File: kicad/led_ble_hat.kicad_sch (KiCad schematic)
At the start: 73 parts, among them J1 USB_C_Receptacle_USB2.0_14P, J2 Battery, J3 Prog, J4 DEBUG, J5 Strip, Q1 2N7002, Q2 AO3401A, Q3 2N7002, Q4 AO3401A, Q5 2N7002, Q6 2N7002, Q7 BSS84, Q8 BSS84, SW1 SW-18010P, U1 TP4054, U2 XC6206P332MR, U3 STM32WB55CGUx, Y1 32Mhz

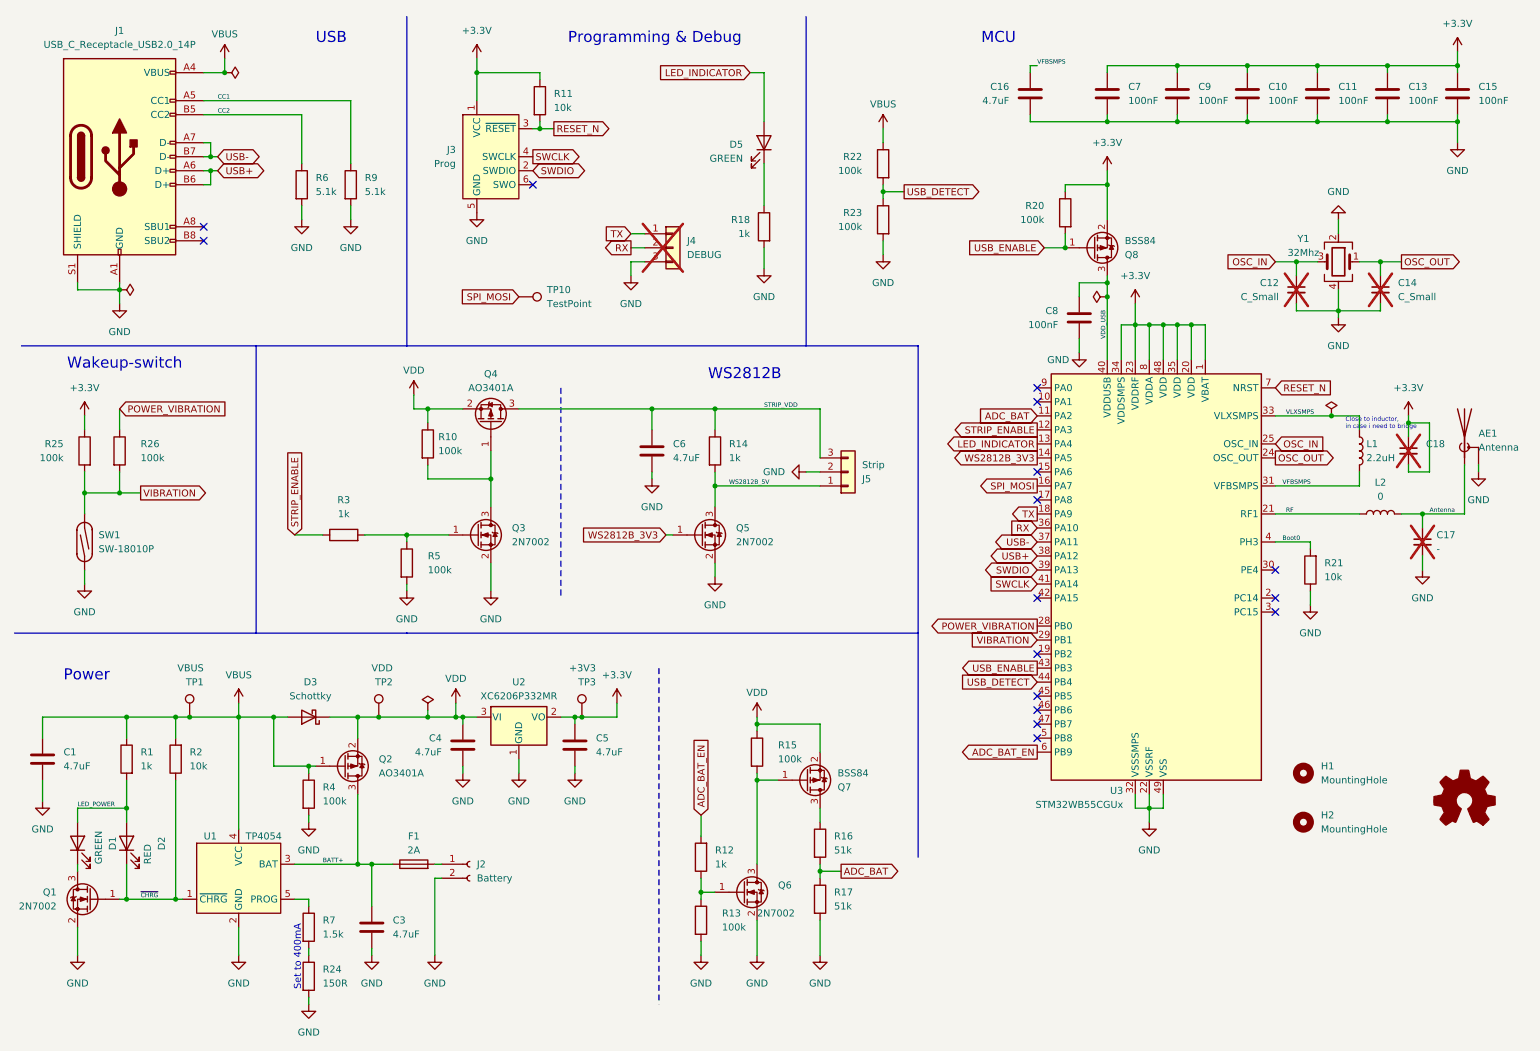
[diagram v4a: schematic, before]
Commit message: Add double inverter for ws2812b output
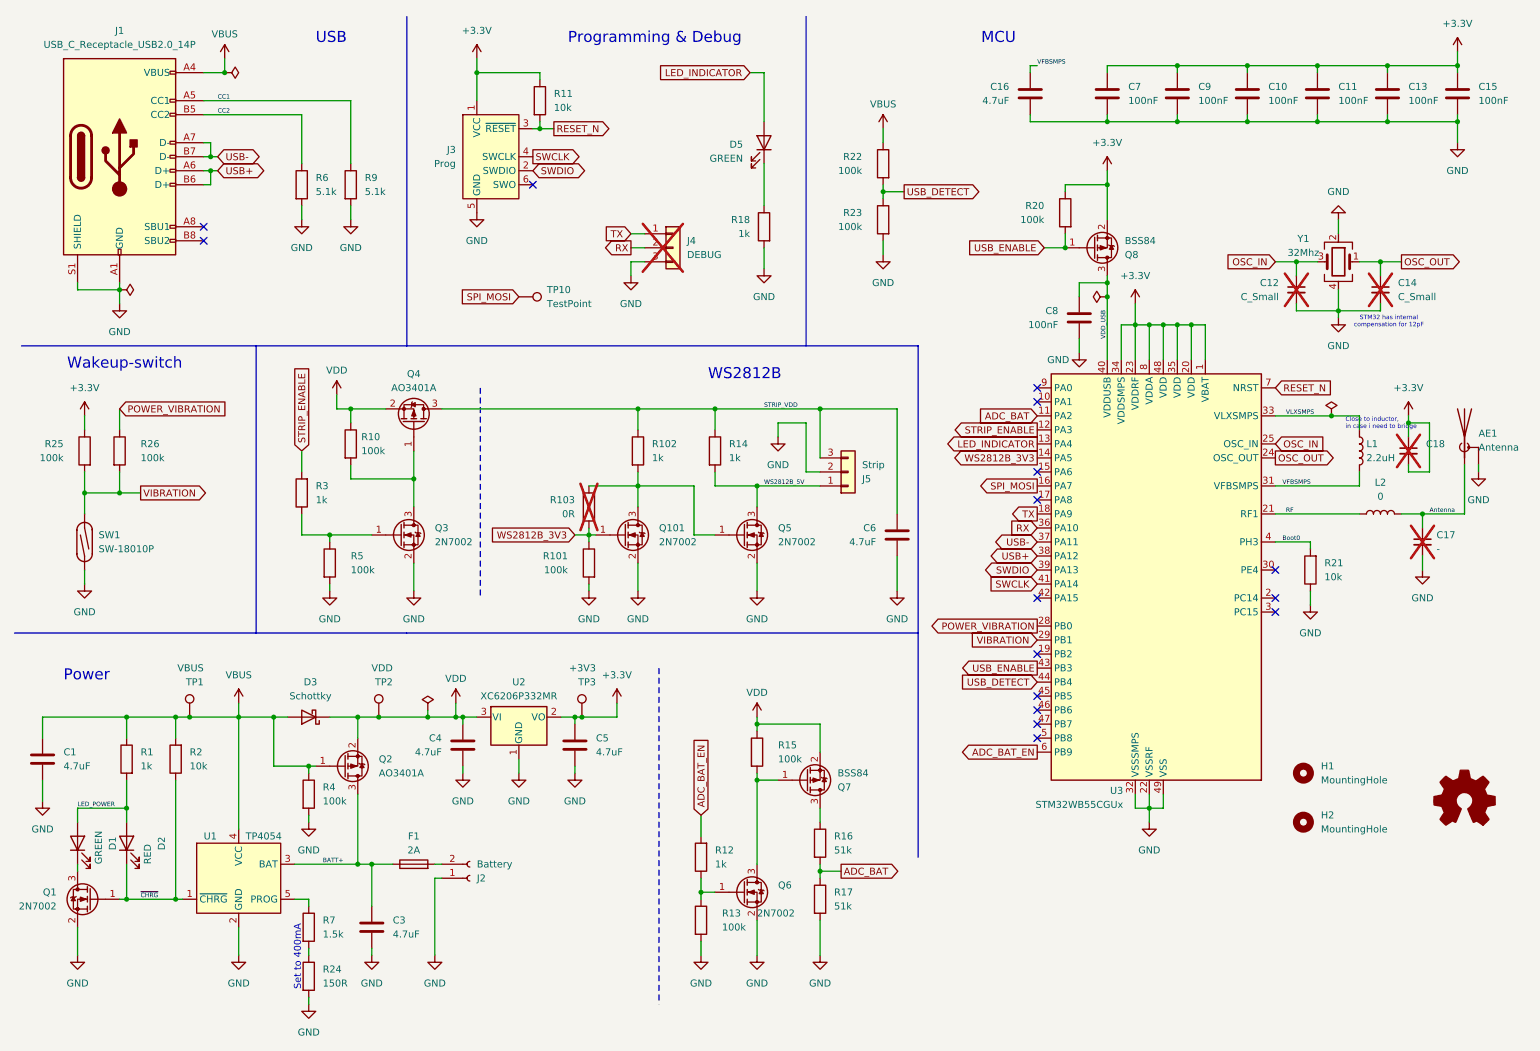
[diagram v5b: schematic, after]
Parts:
- added Q101: 2N7002, Package_TO_SOT_SMD:SOT-23, symbol Transistor_FET:2N7002
- added R101: 100k, Resistor_SMD:R_0402_1005Metric, symbol Device:R
- added R102: 1k, Resistor_SMD:R_0603_1608Metric, symbol Device:R
- added R103: 0R, Resistor_SMD:R_0402_1005Metric, symbol Device:R
- J1: footprint led-hat:GSB1C211110DS1HR -> g-Connector_USB:GSB1C211110DS1HR
- SW1: footprint led-hat:SW-18010P -> g-Sensor_Motion:SW-18010P_Vertical
- U1: symbol led-hat:TP4054-42 -> g-power:TP4054-42
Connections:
- net GND: now also J2.1 (Pin_1), Q101.2 (S), R101.2; no longer J2.2 (Pin_2)
- net STRIP_ENABLE: now also R3.2; no longer R3.1
- net STRIP_VDD: now also R102.1
- net WS2812B_3V3: now also Q101.1 (G), R101.1, R103.1; no longer Q5.1 (G)
- net at F1.2: now also J2.2 (Pin_2); no longer J2.1 (Pin_1)
- net at Q3.1 (G), R5.1: now also R3.1; no longer R3.2
- new net: Q101.3 (D), Q5.1 (G), R102.2, R103.2
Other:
- note added: "STM32 has internal compensation for 12pF"
- moved on the sheet: C6, Q3, Q4, Q5, R10, R3, R5

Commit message: Add accelerometer
Add an accellerometer and gyroscope to maybe add animations and energy
savings based on its output.
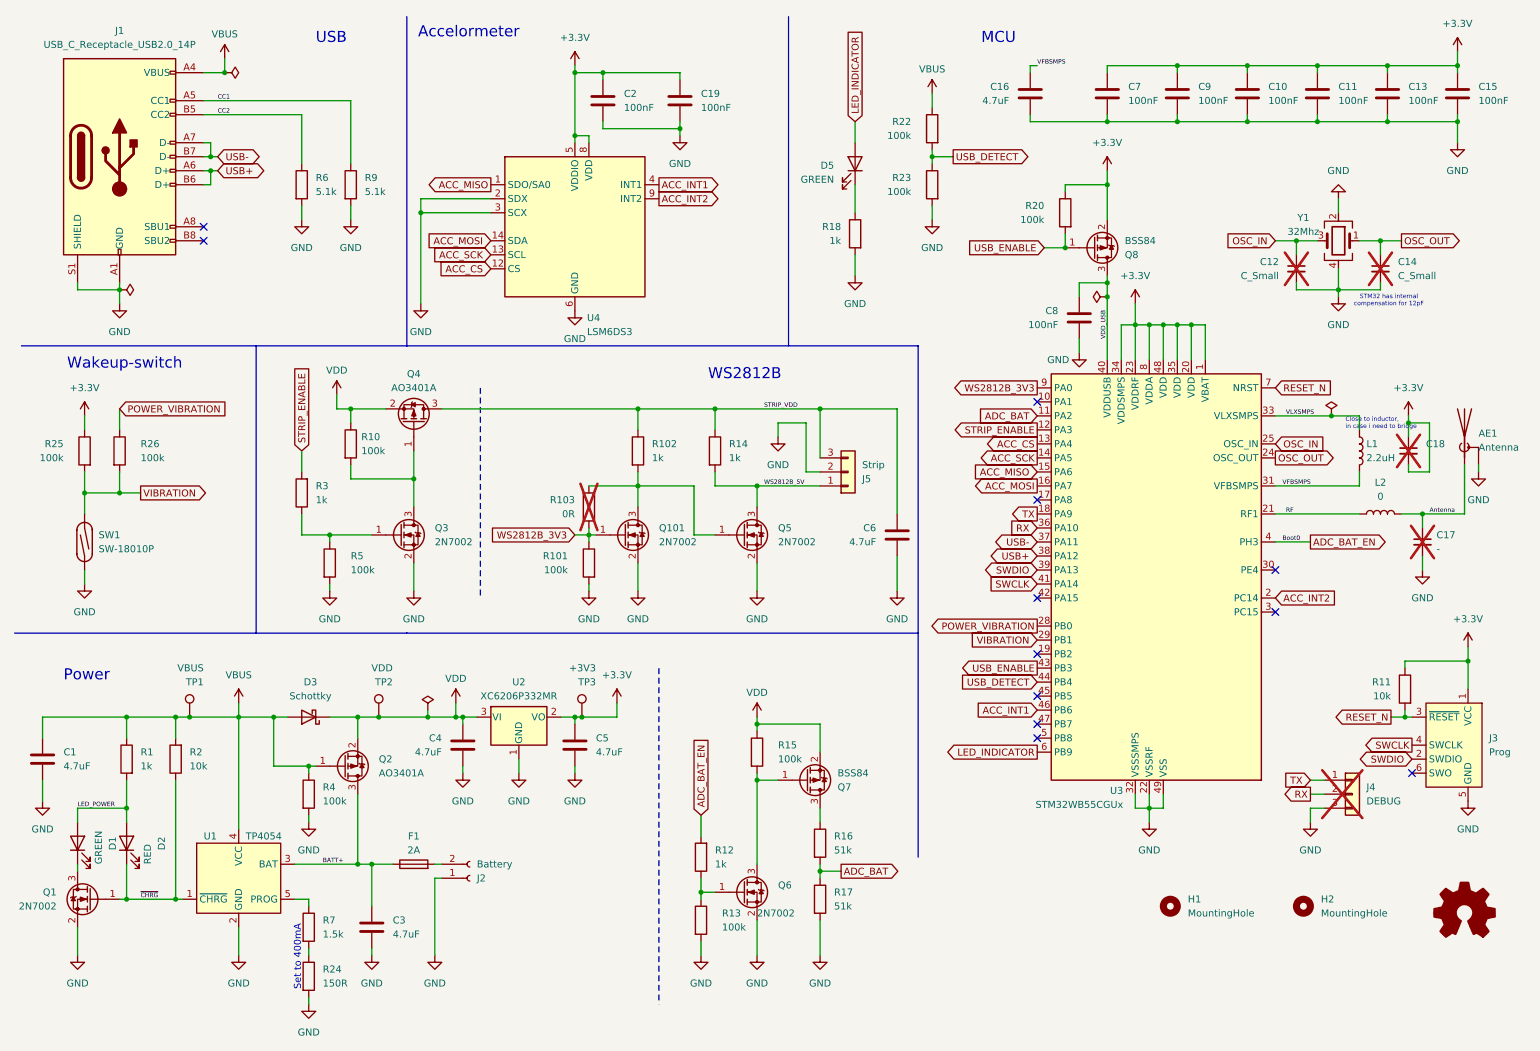
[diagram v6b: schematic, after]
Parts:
- removed R21: 10k, Resistor_SMD:R_0402_1005Metric, symbol Device:R
- removed TP10: TestPoint, TestPoint:TestPoint_Pad_D1.0mm, symbol Connector:TestPoint
- added C19, C2: 100nF, Capacitor_SMD:C_0402_1005Metric, symbol Device:C
- added U4: LSM6DS3, Package_LGA:LGA-14_3x2.5mm_P0.5mm_LayoutBorder3x4y, symbol Sensor_Motion:LSM6DS3
- J4: footprint Connector_PinHeader_2.54mm:PinHeader_1x03_P2.54mm_Vertical -> Connector_PinHeader_2.54mm:PinHeader_1x03_P2.54mm_Vertical_SMD_Pin1Left
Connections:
- net Boot0 is gone; now on net ADC_BAT_EN: U3.4 (PH3)
- net +3.3V: now also C19.2, C2.2, U4.5 (VDDIO), U4.8 (VDD)
- net ADC_BAT_EN: no longer U3.6 (PB9)
- net GND: now also C19.1, C2.1, U4.2 (SDX), U4.3 (SCX), U4.6 (GND), U4.7 (GND)
- net LED_INDICATOR: now also U3.6 (PB9); no longer U3.13 (PA4)
- net WS2812B_3V3: now also U3.9 (PA0); no longer U3.14 (PA5)
- net ACC_MISO: now reaches U3.15 (PA6)
- net ACC_MISO: now also U4.1 (SDO/SA0)
- net ACC_INT2: now reaches U3.2 (PC14)
- net ACC_INT2: now also U4.9 (INT2)
- net ACC_INT1: now reaches U3.46 (PB6)
- net ACC_INT1: now also U4.4 (INT1)
- net SPI_MOSI renamed ACC_MOSI
- net ACC_MOSI: now also U4.14 (SDA)
- new net ACC_CS: U3.13 (PA4), U4.12 (CS)
- new net ACC_SCK: U3.14 (PA5), U4.13 (SCL)
- no-connect marks 16 -> 12
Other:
- note added: "Accelormeter"
- note removed: "Programming & Debug"
- moved on the sheet: C12, C14, D5, H1, H2, J3, J4, R11, R18, R22, R23, Y1

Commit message: Some final touches
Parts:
- AE1, H1, H2, TP1, TP2, TP3: now left out of the parts list
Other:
- note added: "Boot0"
- moved on the sheet: J3, R11
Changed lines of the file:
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@@
 	)
 	(junction
+		(at 265.43 139.7)
+		(diameter 0)
+		(color 0 0 0 0)
+	)
+	(junction
 		(at 119.38 22.86)
 		(diameter 0)
@@
 	)
 	(junction
-		(at 276.225 129.54)
-		(diameter 0)
-		(color 0 0 0 0)
-	)
-	(junction
 		(at 137.16 171.45)
 		(diameter 0)
@@
 	)
 	(junction
-		(at 264.795 139.7)
-		(diameter 0)
-		(color 0 0 0 0)
-	)
-	(junction
 		(at 274.32 31.75)
 		(diameter 0)
@@
 	)
 	(junction
+		(at 276.86 129.54)
+		(diameter 0)
+		(color 0 0 0 0)
+	)
+	(junction
 		(at 48.26 38.1)
 		(diameter 0)
@@
 	)
 	(no_connect
-		(at 266.065 149.86)
+		(at 266.7 149.86)
 	)
 	(no_connect
@@
 	(wire
 		(pts
-			(xy 264.795 129.54) (xy 264.795 130.81)
+			(xy 265.43 129.54) (xy 265.43 130.81)
 		)
 		(stroke
@@
 	(wire
 		(pts
+			(xy 262.89 139.7) (xy 265.43 139.7)
+		)
+		(stroke
+			(width 0)
+			(type default)
+		)
+	)
+	(wire
+		(pts
 			(xy 236.22 22.86) (xy 236.22 21.59)
 		)
@@
 	(wire
 		(pts
-			(xy 276.225 129.54) (xy 264.795 129.54)
+			(xy 265.43 129.54) (xy 276.86 129.54)
 		)
 		(stroke
@@
 	(wire
 		(pts
+			(xy 265.43 139.7) (xy 266.7 139.7)
+		)
+		(stroke
+			(width 0)
+			(type default)
+		)
+	)
+	(wire
+		(pts
 			(xy 267.97 102.87) (xy 275.59 102.87)
 		)
@@
 	(wire
 		(pts
-			(xy 276.225 127) (xy 276.225 129.54)
+			(xy 276.86 127) (xy 276.86 129.54)
 		)
 		(stroke
@@
 	(wire
 		(pts
-			(xy 264.795 139.7) (xy 262.255 139.7)
-		)
-		(stroke
-			(width 0)
-			(type default)
-		)
-	)
-	(wire
-		(pts
 			(xy 116.84 105.41) (xy 116.84 106.68)
 		)
@@
 	(wire
 		(pts
-			(xy 276.225 129.54) (xy 276.225 134.62)
+			(xy 276.86 129.54) (xy 276.86 134.62)
 		)
 		(stroke
@@
 	(wire
 		(pts
-			(xy 264.795 138.43) (xy 264.795 139.7)
+			(xy 265.43 138.43) (xy 265.43 139.7)
 		)
 		(stroke
@@
 	(wire
 		(pts
-			(xy 264.795 139.7) (xy 266.065 139.7)
-		)
-		(stroke
-			(width 0)
-			(type default)
-		)
-	)
-	(wire
-		(pts
 			(xy 158.75 166.37) (xy 158.75 167.64)
 		)
@@
 		)
 	)
+	(text "Boot0"
+		(exclude_from_sim no)
+		(at 244.094 107.442 0)
+		(effects
+			(font
+				(size 0.8 0.8)
+			)
+		)
+	)
 	(text "STM32 has internal\ncompensation for 12pF"
 		(exclude_from_sim no)
@@
 		)
 	)
-	(label "Boot0"
-		(at 242.57 107.95 0)
-		(fields_autoplaced yes)
-		(effects
-			(font
-				(size 0.8 0.8)
-			)
-			(justify left bottom)
-		)
-	)
 	(label "VFBSMPS"
 		(at 198.12 21.59 0)
@@
 	(global_label "SWDIO"
 		(shape bidirectional)
-		(at 266.065 147.32 180)
+		(at 266.7 147.32 180)
 		(fields_autoplaced yes)
 		(effects
@@
 		)
 		(property "Intersheetrefs" "${INTERSHEET_REFS}"
-			(at 256.1023 147.32 0)
+			(at 256.7373 147.32 0)
 			(effects
 				(font
@@
 	(global_label "SWCLK"
 		(shape output)
-		(at 266.065 144.78 180)
+		(at 266.7 144.78 180)
 		(fields_autoplaced yes)
 		(effects
@@
 		)
 		(property "Intersheetrefs" "${INTERSHEET_REFS}"
-			(at 256.8508 144.78 0)
+			(at 257.4858 144.78 0)
 			(effects
 				(font
@@
 	(global_label "RESET_N"
 		(shape output)
-		(at 262.255 139.7 180)
+		(at 262.89 139.7 180)
 		(fields_autoplaced yes)
 		(effects
@@
 		)
 		(property "Intersheetrefs" "${INTERSHEET_REFS}"
-			(at 251.2266 139.7 0)
+			(at 251.8616 139.7 0)
 			(effects
 				(font
@@
 		(unit 1)
 		(exclude_from_sim no)
-		(in_bom yes)
+		(in_bom no)
 		(on_board yes)
 		(dnp no)
@@
 		(unit 1)
 		(exclude_from_sim no)
-		(in_bom yes)
+		(in_bom no)
 		(on_board yes)
 		(dnp no)
@@
 		(unit 1)
 		(exclude_from_sim no)
-		(in_bom yes)
+		(in_bom no)
 		(on_board yes)
 		(dnp no)
@@
 	(symbol
 		(lib_id "power:GND")
-		(at 276.225 154.94 0)
+		(at 276.86 154.94 0)
 		(mirror y)
 		(unit 1)
@@
 		(fields_autoplaced yes)
 		(property "Reference" "#PWR019"
-			(at 276.225 161.29 0)
+			(at 276.86 161.29 0)
 			(effects
 				(font
@@
 		)
 		(property "Value" "GND"
-			(at 276.225 160.02 0)
+			(at 276.86 160.02 0)
 			(effects
 				(font
@@
 		)
 		(property "Footprint" ""
-			(at 276.225 154.94 0)
+			(at 276.86 154.94 0)
 			(effects
 				(font
@@
 		)
 		(property "Datasheet" ""
-			(at 276.225 154.94 0)
+			(at 276.86 154.94 0)
 			(effects
 				(font
@@
 		)
 		(property "Description" "Power symbol creates a global label with name \"GND\" , ground"
-			(at 276.225 154.94 0)
+			(at 276.86 154.94 0)
 			(effects
 				(font
@@
 		(unit 1)
 		(exclude_from_sim no)
-		(in_bom yes)
+		(in_bom no)
 		(on_board yes)
 		(dnp no)
@@
 		(unit 1)
 		(exclude_from_sim no)
-		(in_bom yes)
+		(in_bom no)
 		(on_board yes)
 		(dnp no)
@@
 	(symbol
 		(lib_id "Device:R")
-		(at 264.795 134.62 0)
+		(at 265.43 134.62 0)
 		(mirror y)
 		(unit 1)
@@
 		(fields_autoplaced yes)
 		(property "Reference" "R11"
-			(at 262.255 133.35 0)
+			(at 262.89 133.35 0)
 			(effects
 				(font
@@
 		)
 		(property "Value" "10k"
-			(at 262.255 135.89 0)
+			(at 262.89 135.89 0)
 			(effects
 				(font
@@
 		)
 		(property "Footprint" "Resistor_SMD:R_0402_1005Metric"
-			(at 266.573 134.62 90)
+			(at 267.208 134.62 90)
 			(effects
 				(font
@@
 		)
 		(property "Datasheet" "~"
-			(at 264.795 134.62 0)
+			(at 265.43 134.62 0)
 			(effects
 				(font
@@
 		)
 		(property "Description" ""
-			(at 264.795 134.62 0)
+			(at 265.43 134.62 0)
 			(effects
 				(font
@@
 		)
 		(property "LCSC#" "C25744"
-			(at 264.795 134.62 0)
+			(at 265.43 134.62 0)
 			(effects
 				(font
@@
 	(symbol
 		(lib_id "Connector:Conn_ARM_SWD_TagConnect_TC2030-NL")
-		(at 273.685 144.78 0)
+		(at 274.32 144.78 0)
 		(mirror y)
 		(unit 1)
@@
 		(fields_autoplaced yes)
 		(property "Reference" "J3"
-			(at 280.035 143.51 0)
+			(at 280.67 143.51 0)
 			(effects
 				(font
@@
 		)
 		(property "Value" "Prog"
-			(at 280.035 146.05 0)
+			(at 280.67 146.05 0)
 			(effects
 				(font
@@
 		)
 		(property "Footprint" "Connector:Tag-Connect_TC2030-IDC-NL_2x03_P1.27mm_Vertical"
-			(at 273.685 162.56 0)
+			(at 274.32 162.56 0)
 			(effects
 				(font
@@
 		)
 		(property "Datasheet" "https://www.tag-connect.com/wp-content/uploads/bsk-pdf-manager/TC2030-CTX_1.pdf"
-			(at 273.685 160.02 0)
+			(at 274.32 160.02 0)
 			(effects
 				(font
@@
 		)
 		(property "Description" ""
-			(at 273.685 144.78 0)
+			(at 274.32 144.78 0)
 			(effects
 				(font
@@
 		)
 		(property "LCSC#" "-"
-			(at 273.685 144.78 0)
+			(at 274.32 144.78 0)
 			(effects
 				(font
@@
 		(unit 1)
 		(exclude_from_sim no)
-		(in_bom yes)
+		(in_bom no)
 		(on_board yes)
 		(dnp no)
@@
 	(symbol
 		(lib_id "power:+3.3V")
-		(at 276.225 127 0)
+		(at 276.86 127 0)
 		(mirror y)
 		(unit 1)
@@
 		(fields_autoplaced yes)
 		(property "Reference" "#PWR018"
-			(at 276.225 130.81 0)
+			(at 276.86 130.81 0)
 			(effects
 				(font
@@
 		)
 		(property "Value" "+3.3V"
-			(at 276.225 121.92 0)
+			(at 276.86 121.92 0)
 			(effects
 				(font
@@
 		)
 		(property "Footprint" ""
-			(at 276.225 127 0)
+			(at 276.86 127 0)
 			(effects
 				(font
@@
 		)
 		(property "Datasheet" ""
-			(at 276.225 127 0)
+			(at 276.86 127 0)
 			(effects
 				(font
@@
 		)
 		(property "Description" "Power symbol creates a global label with name \"+3.3V\""
-			(at 276.225 127 0)
+			(at 276.86 127 0)
 			(effects
 				(font
